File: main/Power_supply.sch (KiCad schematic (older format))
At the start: 38 parts, among them IC2 TPS54294PWP, IC3 TPS54294PWP, J7 External +1V8, J8 External +1V0, J9 External +3.3V

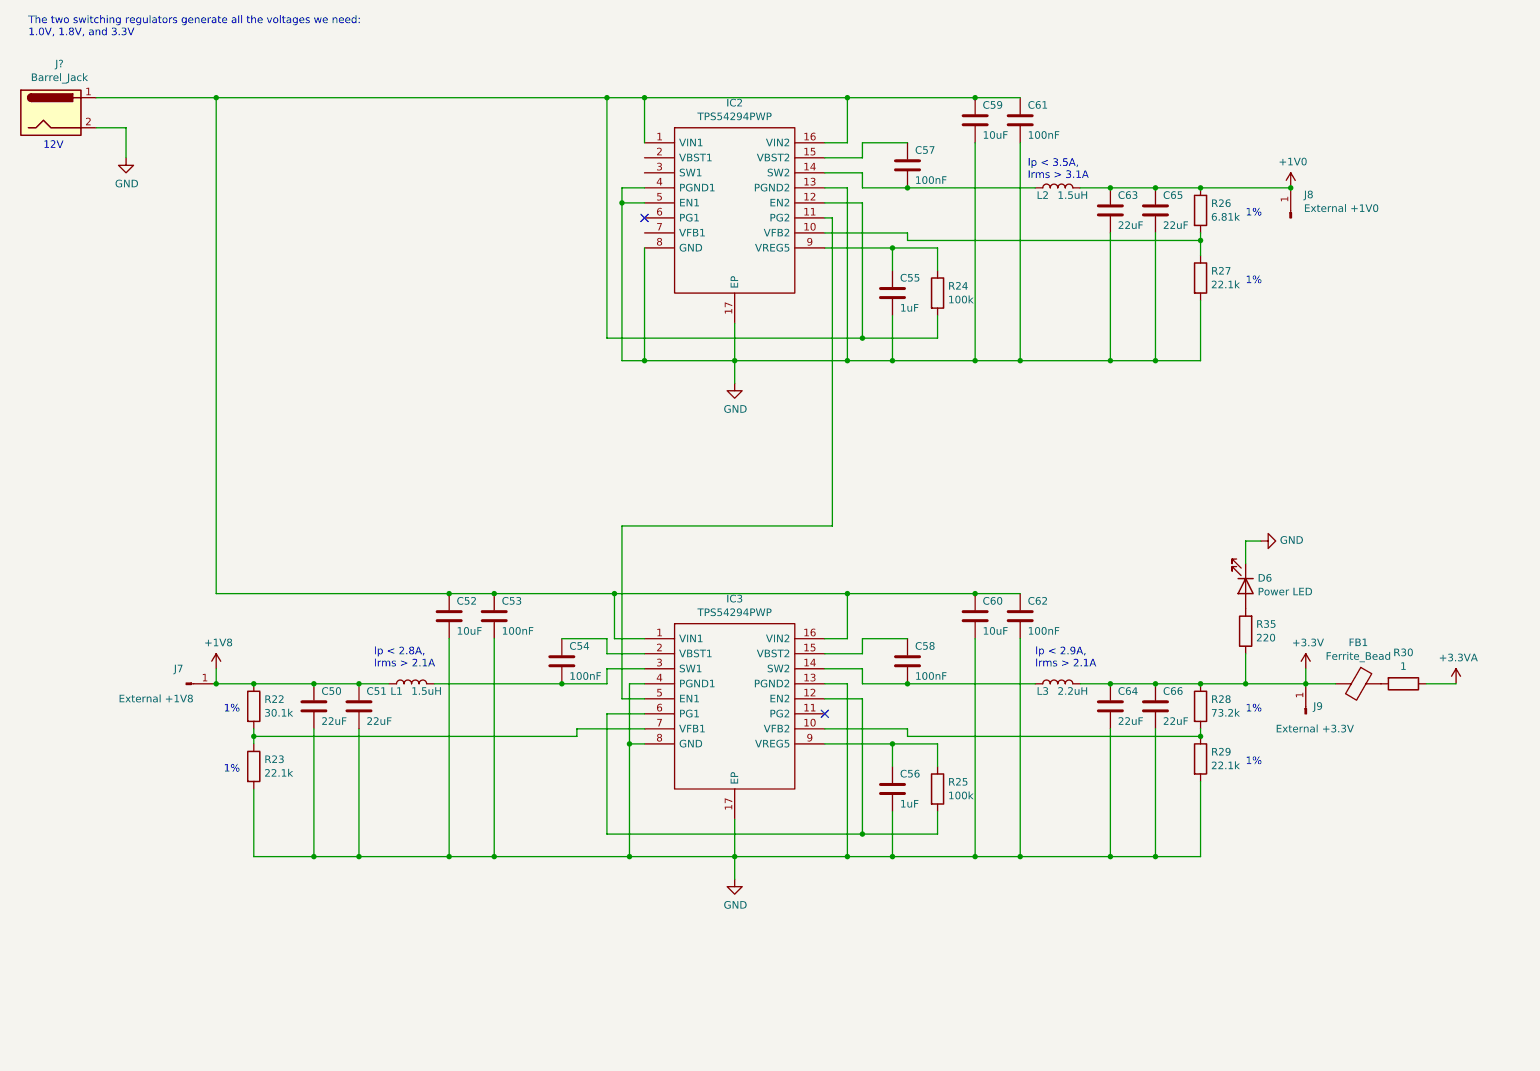
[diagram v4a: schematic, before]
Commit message: Add FPGA RAM chip
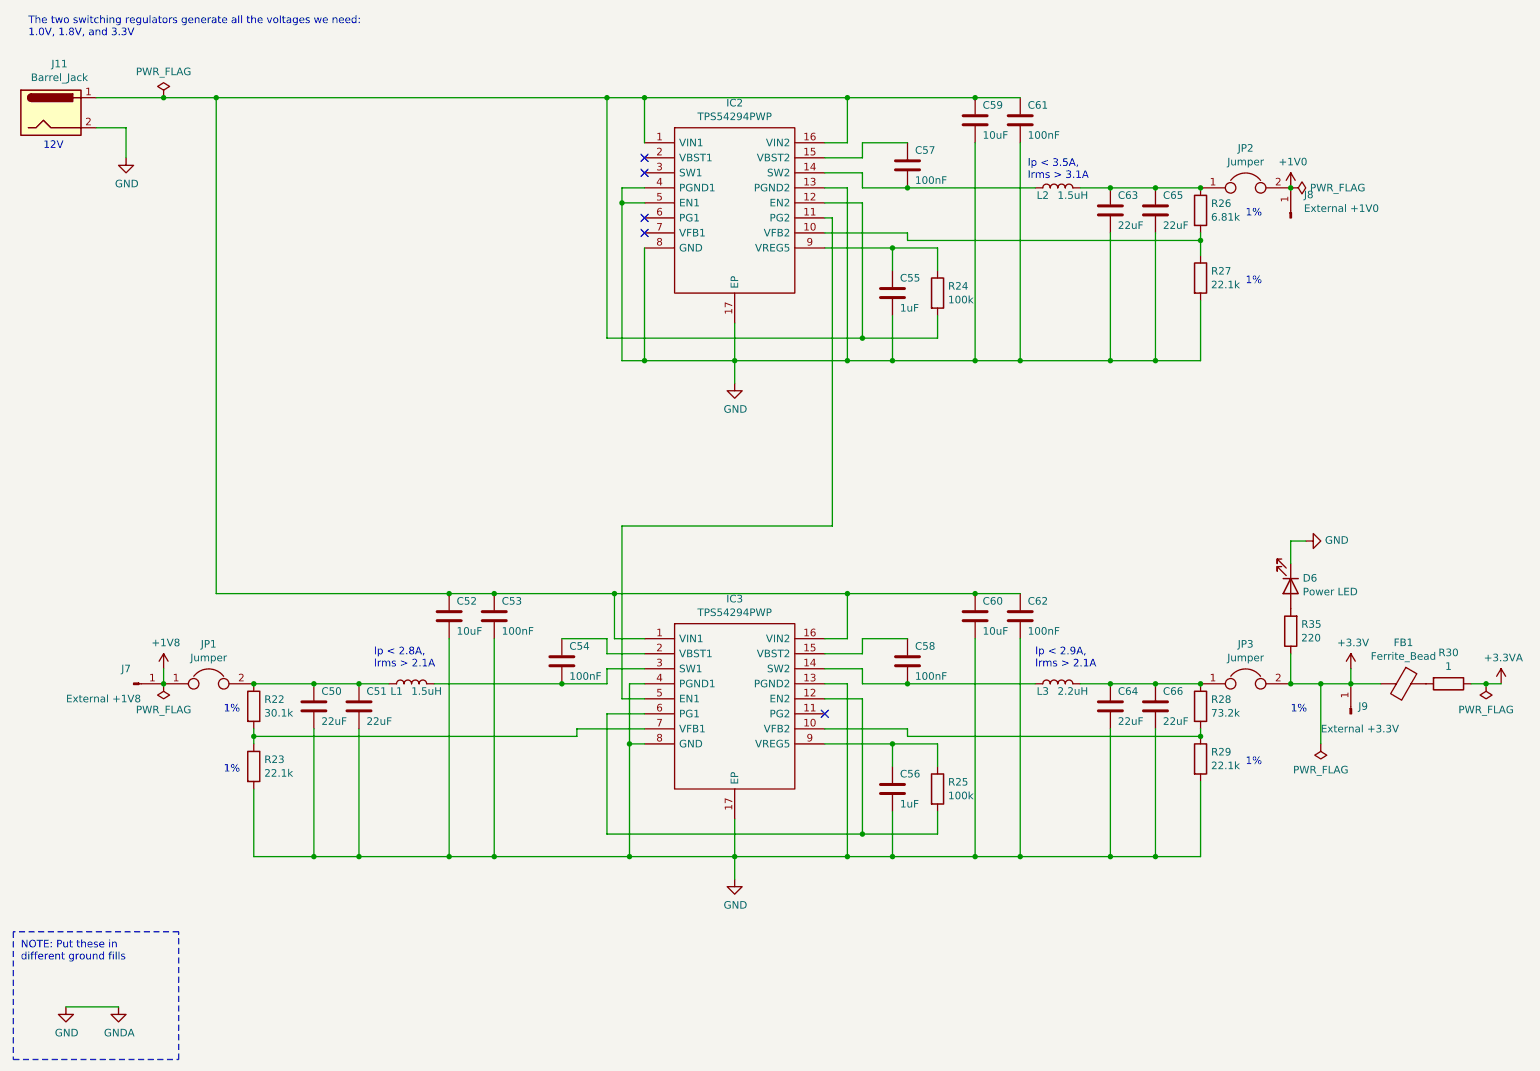
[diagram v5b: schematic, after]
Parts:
- added JP1, JP2, JP3: Jumper, symbol Device:Jumper
- gave numbers to parts that had none: 1
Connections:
- net +1V0: now also JP2.2; no longer C63.1, C65.1, L2.2, R26.1
- net +1V8: now also JP1.1; no longer C50.1, C51.1, L1.1, R22.1
- net +3V3: now also JP3.2; no longer C64.1, C66.1, L3.2, R28.1
- new net: C50.1, C51.1, JP1.2, L1.1, R22.1
- new net: C64.1, C66.1, JP3.1, L3.2, R28.1
- new net: C63.1, C65.1, JP2.1, L2.2, R26.1
- no-connect marks 2 -> 5
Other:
- note added: "NOTE: Put these in \ndifferent ground fills\n"
- moved on the sheet: D6, FB1, J7, J9, R30, R35

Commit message: Final cleanup before sending in for rebiew
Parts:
- renumbered C52 to C10, C53 to C11, C54 to C12, C55 to C13, C56 to C14, C57 to C15, C58 to C16, C59 to C17, C60 to C18, C61 to C19, C62 to C20, C63 to C21, C64 to C22, C65 to C23, C66 to C24, C50 to C8, C51 to C9, D6 to D2, IC2 to IC1, IC3 to IC2, J11 to J3, J7 to J4, J8 to J5, J9 to J6, R22 to R12, R23 to R13, R24 to R14, R25 to R15, R26 to R16, R27 to R17, R28 to R18, R29 to R19, R35 to R20, R30 to R21

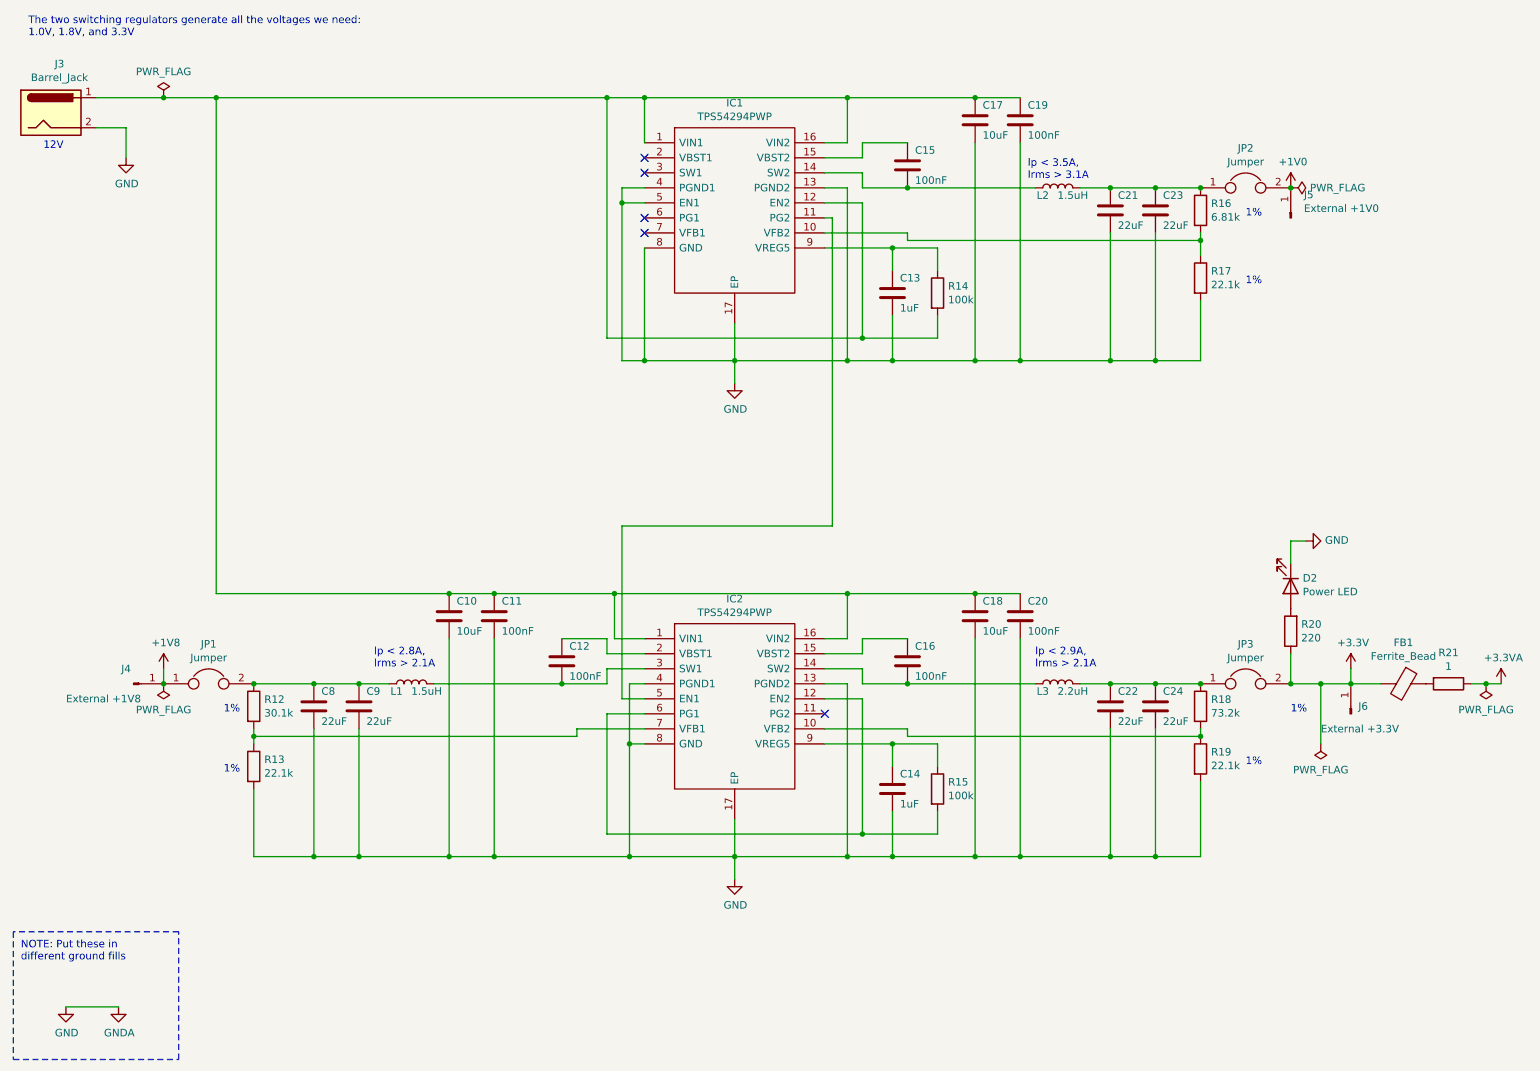
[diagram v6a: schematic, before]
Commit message: Fix up after review
Done:
- Add bulk decoupling capacitor to switch regulator cirucit
- Disconnect DONE from PROGRAM_B in FPGA (mistake)
- The decoupling capacitors used for the FPGA were for the 15T, not the
  100T. It was also setup for two I/O banks, we only use one. Disconnect
  I/O bank 15.
- Switch external clock on the MCU to an oscillator, allowing for 72MHz
- Switch pinout of the backup SPI on the MCU so that half the pins are
  ground

Mizzing:
- Add low-pass filters to the output of the DAC as per the datasheet.
  May remove the need for the amplifier circuit.
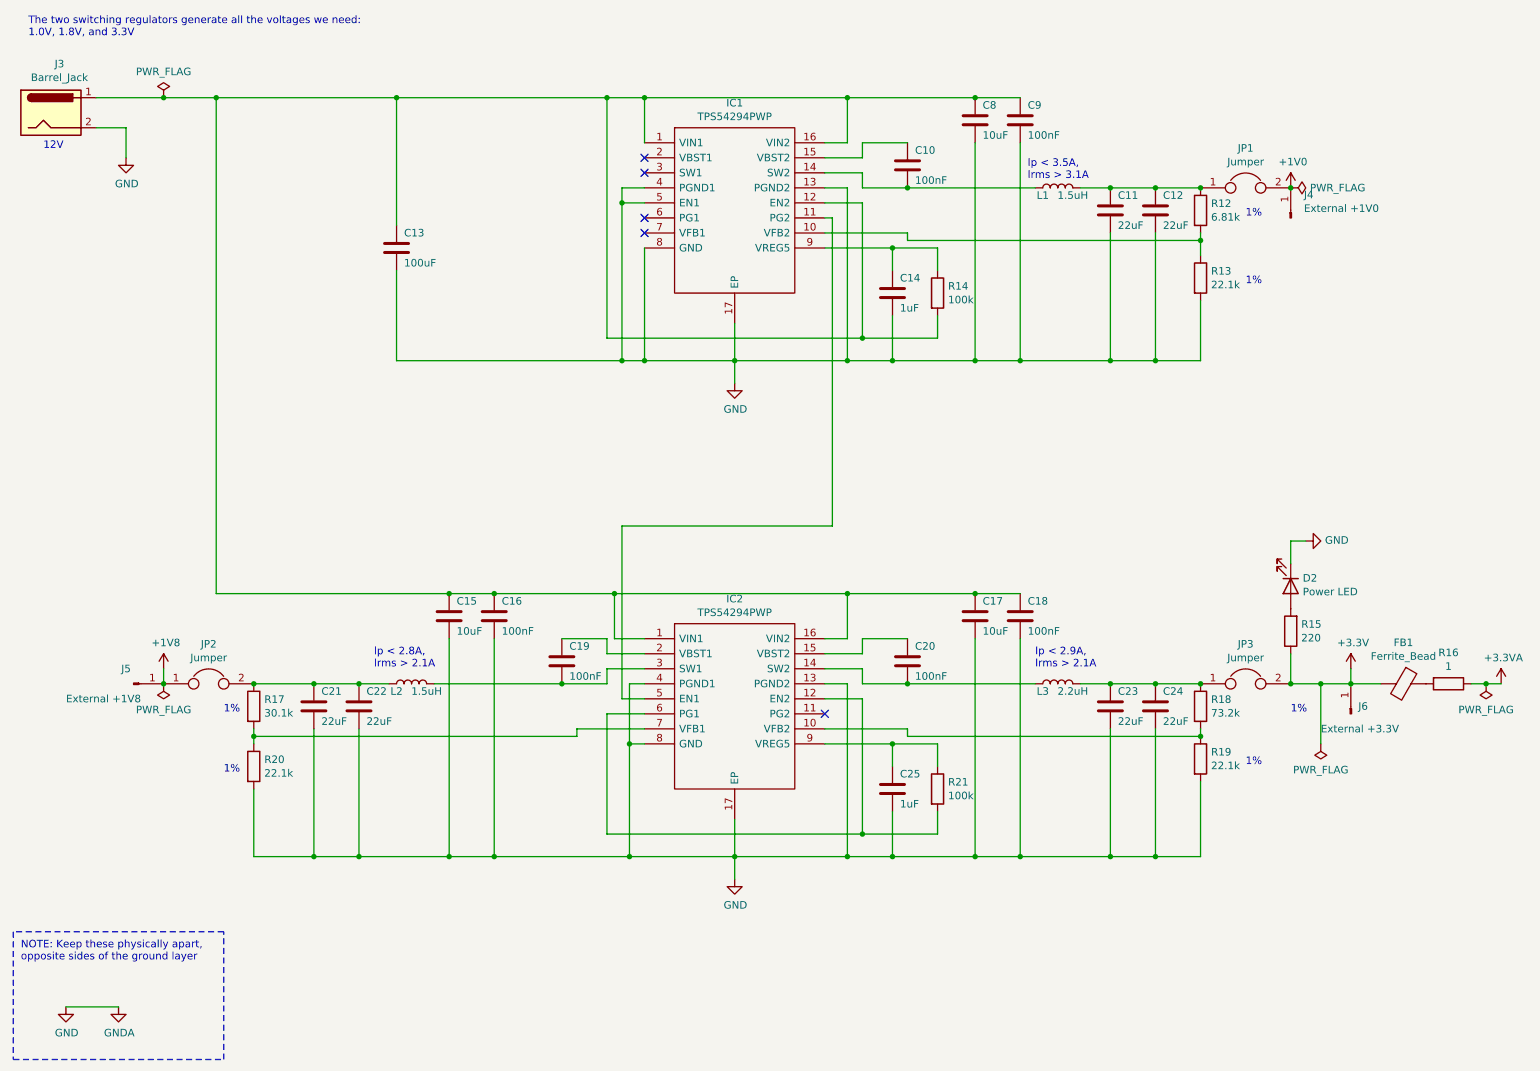
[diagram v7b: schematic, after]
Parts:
- added C13: 100uF, Resistor_SMD:R_1210_3225Metric_Pad1.30x2.65mm_HandSolder, symbol Device:C
- D2: footprint (none) -> LED_SMD:LED_0805_2012Metric_Pad1.15x1.40mm_HandSolder
- R12: renamed from R16; footprint (none) -> Resistor_SMD:R_0805_2012Metric_Pad1.20x1.40mm_HandSolder
- R13: renamed from R17; footprint (none) -> Resistor_SMD:R_0805_2012Metric_Pad1.20x1.40mm_HandSolder
- R14, R18, R19: footprint (none) -> Resistor_SMD:R_0805_2012Metric_Pad1.20x1.40mm_HandSolder
- R15: renamed from R20; footprint (none) -> Resistor_SMD:R_0805_2012Metric_Pad1.20x1.40mm_HandSolder
- R16: renamed from R21; footprint (none) -> Resistor_SMD:R_0805_2012Metric_Pad1.20x1.40mm_HandSolder
- R17: renamed from R12; footprint (none) -> Resistor_SMD:R_0805_2012Metric_Pad1.20x1.40mm_HandSolder
- R20: renamed from R13; footprint (none) -> Resistor_SMD:R_0805_2012Metric_Pad1.20x1.40mm_HandSolder
- R21: renamed from R15; footprint (none) -> Resistor_SMD:R_0805_2012Metric_Pad1.20x1.40mm_HandSolder
- renumbered C15 to C10, C21 to C11, C23 to C12, C13 to C14, C10 to C15, C11 to C16, C18 to C17, C20 to C18, C12 to C19, C16 to C20, C8 to C21, C9 to C22, C22 to C23, C14 to C25, C17 to C8, C19 to C9, J5 to J4, J4 to J5, JP2 to JP1, JP1 to JP2, L2 to L1, L1 to L2
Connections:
- net GND: now also C13.2
- net at C15.1, C16.1, C17.1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: now also C13.1
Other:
- note added: "NOTE: Keep these physically apart,\nopposite sides of the ground layer"
- note removed: "NOTE: Put these in \ndifferent ground fills\n"

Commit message: Fix up after review 3
Add +3.3V and GND to MCU and FPGA GPIO.

Add a lot of footprints.
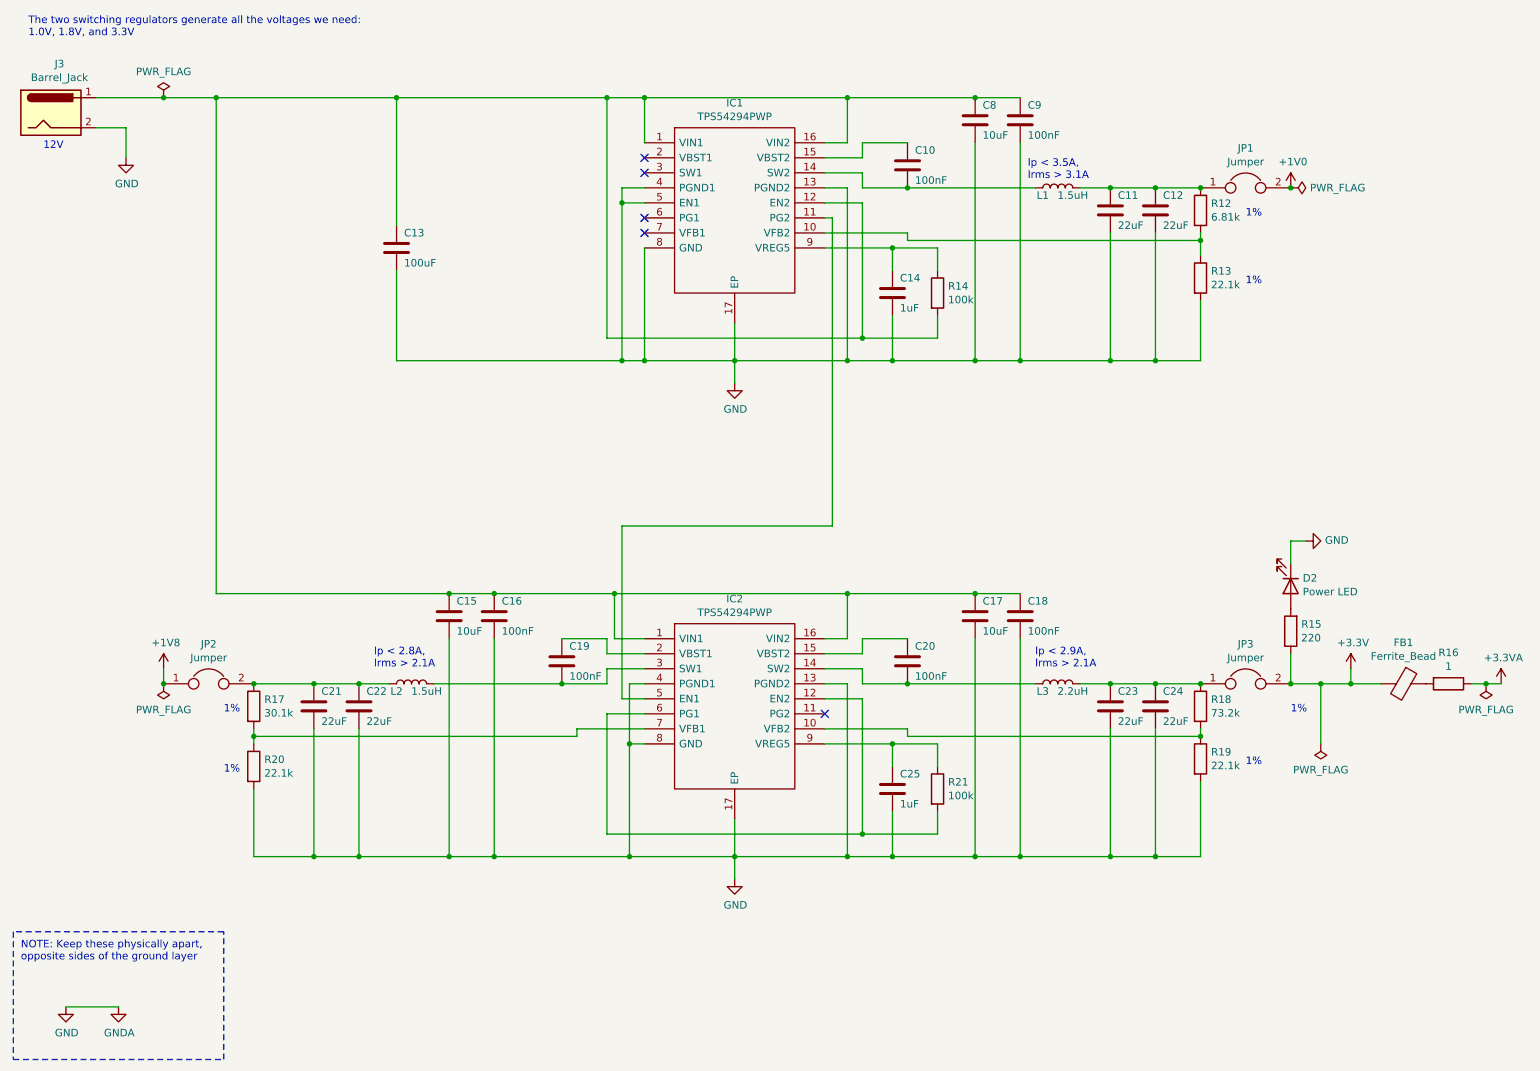
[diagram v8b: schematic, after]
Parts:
- removed J4: External +1V0, symbol Connector:Conn_01x01_Male
- removed J5: External +1V8, symbol Connector:Conn_01x01_Male
- removed J6: External +3.3V, symbol Connector:Conn_01x01_Male
- C13: footprint Resistor_SMD:R_1210_3225Metric_Pad1.30x2.65mm_HandSolder -> Capacitor_SMD:C_1210_3225Metric_Pad1.33x2.70mm_HandSolder
- L1, L2, L3: footprint (none) -> Inductor_SMD:L_1806_4516Metric_Pad1.57x1.80mm_HandSolder
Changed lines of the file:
@@
 F 0 "L2" V 3250 5300 50  0000 C CNN
 F 1 "1.5uH" V 3250 5100 50  0000 C CNN
-F 2 "" H 3300 5200 50  0001 C CNN
+F 2 "Inductor_SMD:L_1806_4516Metric_Pad1.57x1.80mm_HandSolder" H 3300 5200 50  0001 C CNN
 F 3 "~" H 3300 5200 50  0001 C CNN
 	1    3300 5200
@@
 F 0 "L3" V 7550 5300 50  0000 C CNN
 F 1 "2.2uH" V 7550 5100 50  0000 C CNN
-F 2 "" H 7600 5200 50  0001 C CNN
+F 2 "Inductor_SMD:L_1806_4516Metric_Pad1.57x1.80mm_HandSolder" H 7600 5200 50  0001 C CNN
 F 3 "~" H 7600 5200 50  0001 C CNN
 	1    7600 5200
@@
 F 0 "L1" V 7550 2000 50  0000 C CNN
 F 1 "1.5uH" V 7550 1800 50  0000 C CNN
-F 2 "" H 7600 1900 50  0001 C CNN
+F 2 "Inductor_SMD:L_1806_4516Metric_Pad1.57x1.80mm_HandSolder" H 7600 1900 50  0001 C CNN
 F 3 "~" H 7600 1900 50  0001 C CNN
 	1    7600 1900
@@
 	9150 4250 9250 4250
 Connection ~ 9550 5200
-$Comp
-L Connector:Conn_01x01_Male J5
-U 1 1 6189543E
-P 1450 5200
-F 0 "J5" H 1400 5300 50  0000 C CNN
-F 1 "External +1V8" H 1250 5100 50  0000 C CNN
-F 2 "" H 1450 5200 50  0001 C CNN
-F 3 "~" H 1450 5200 50  0001 C CNN
-	1    1450 5200
-	1    0    0    -1
-$EndComp
-$Comp
-L Connector:Conn_01x01_Male J6
-U 1 1 61895F3D
-P 9550 5400
-F 0 "J6" V 9600 5350 50  0000 R CNN
-F 1 "External +3.3V" V 9450 5600 50  0000 R CNN
-F 2 "" H 9550 5400 50  0001 C CNN
-F 3 "~" H 9550 5400 50  0001 C CNN
-	1    9550 5400
-	0    -1   -1   0
-$EndComp
-$Comp
-L Connector:Conn_01x01_Male J4
-U 1 1 61896E72
-P 9150 2100
-F 0 "J4" V 9304 2012 50  0000 R CNN
-F 1 "External +1V0" V 9213 2012 50  0000 R CNN
-F 2 "" H 9150 2100 50  0001 C CNN
-F 3 "~" H 9150 2100 50  0001 C CNN
-	1    9150 2100
-	0    -1   -1   0
-$EndComp
 Connection ~ 9150 1900
 $Comp
@@
 F 0 "C13" H 3250 2400 50  0000 L CNN
 F 1 "100uF" H 3250 2200 50  0000 L CNN
-F 2 "Resistor_SMD:R_1210_3225Metric_Pad1.30x2.65mm_HandSolder" H 3238 2150 50  0001 C CNN
+F 2 "Capacitor_SMD:C_1210_3225Metric_Pad1.33x2.70mm_HandSolder" H 3238 2150 50  0001 C CNN
 F 3 "~" H 3200 2300 50  0001 C CNN
 	1    3200 2300
